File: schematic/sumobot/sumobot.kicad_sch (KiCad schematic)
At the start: 30 parts, among them J1 Conn_02x09_Odd_Even, J2 Conn_01x03, J3 Conn_02x06_Counter_Clockwise, J4 Conn_01x02_Socket, J5 Conn_01x02_Socket, J6 Conn_01x02_Socket, J7 Conn_01x07, SW3 SW_DIP_x04, U1 ROB-14450, U10 VL53L0CXV0DH1, U11 ESP32-DEVKITC-32D, U2 YAAJ_DCDC_StepDown_LM2596, U4 TPR-105F, U5 VL53L0CXV0DH1, U6 TPR-105F, U7 TPR-105F, U8 TPR-105F, U9 VL53L0CXV0DH1

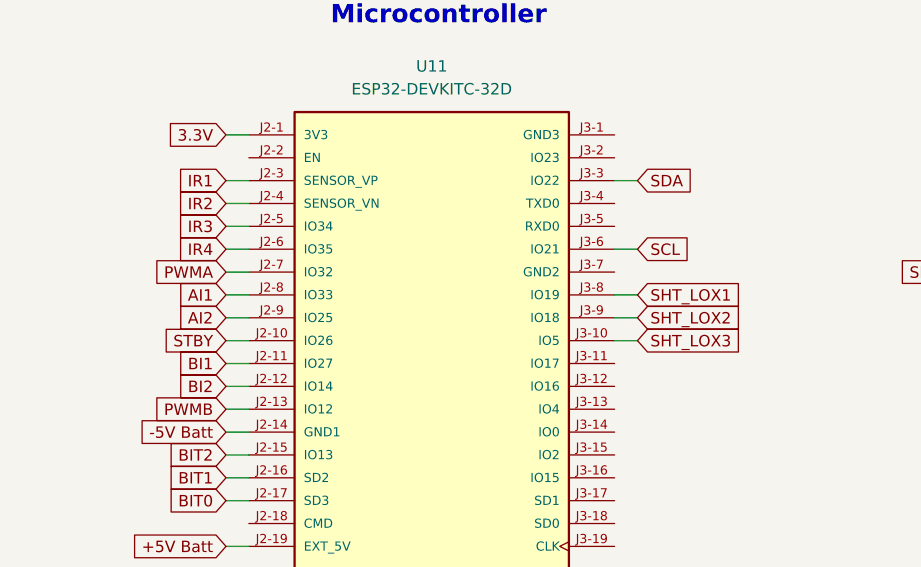
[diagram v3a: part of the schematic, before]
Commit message: feat: enhance main control logic with new sensor integration and strategy adjustments
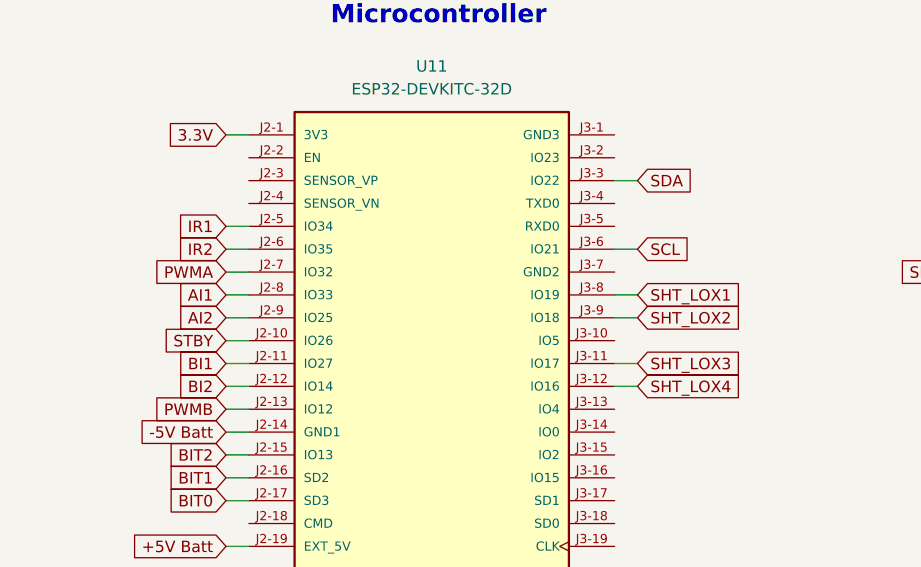
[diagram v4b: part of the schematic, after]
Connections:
- net IR1: now also U11.J2-5 (IO34); no longer U11.J2-3 (SENSOR_VP)
- net IR2: now also U11.J2-6 (IO35); no longer U11.J2-4 (SENSOR_VN)
- net IR3: no longer U11.J2-5 (IO34)
- net IR4: no longer U11.J2-6 (IO35)
- net SHT_LOX3: now also U11.J3-11 (IO17); no longer U11.J3-10 (IO5)
- net SHT_LOX4: now reaches U11.J3-12 (IO16)
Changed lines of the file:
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@@
 	(wire
 		(pts
+			(xy 176.53 215.9) (xy 179.07 215.9)
+		)
+		(stroke
+			(width 0)
+			(type default)
+		)
+	)
+	(wire
+		(pts
 			(xy 30.48 166.37) (xy 33.02 166.37)
 		)
@@
 	(wire
 		(pts
-			(xy 179.07 210.82) (xy 176.53 210.82)
-		)
-		(stroke
-			(width 0)
-			(type default)
-		)
-	)
-	(wire
-		(pts
 			(xy 233.68 162.56) (xy 234.95 162.56)
 		)
@@
 	(wire
 		(pts
+			(xy 176.53 213.36) (xy 179.07 213.36)
+		)
+		(stroke
+			(width 0)
+			(type default)
+		)
+	)
+	(wire
+		(pts
 			(xy 85.09 87.63) (xy 86.36 87.63)
 		)
@@
 	(wire
 		(pts
-			(xy 133.35 193.04) (xy 135.89 193.04)
-		)
-		(stroke
-			(width 0)
-			(type default)
-		)
-	)
-	(wire
-		(pts
 			(xy 133.35 215.9) (xy 135.89 215.9)
 		)
@@
 	(wire
 		(pts
-			(xy 133.35 195.58) (xy 135.89 195.58)
-		)
-		(stroke
-			(width 0)
-			(type default)
-		)
-	)
-	(wire
-		(pts
 			(xy 232.41 180.34) (xy 233.68 180.34)
 		)
@@
 		)
 	)
-	(global_label "IR1"
-		(shape input)
-		(at 133.35 193.04 180)
-		(fields_autoplaced yes)
-		(effects
-			(font
-				(size 1.27 1.27)
-			)
-			(justify right)
-		)
-		(property "Intersheetrefs" "${INTERSHEET_REFS}"
-			(at 127.2805 193.04 0)
-			(effects
-				(font
-					(size 1.27 1.27)
-				)
-				(justify right)
-				(hide yes)
-			)
-		)
-	)
 	(global_label "AO2"
 		(shape input)
@@
 		)
 	)
-	(global_label "IR4"
+	(global_label "IR2"
 		(shape input)
 		(at 133.35 200.66 180)
@@
 		)
 	)
+	(global_label "SHT_LOX4"
+		(shape input)
+		(at 179.07 215.9 0)
+		(fields_autoplaced yes)
+		(effects
+			(font
+				(size 1.27 1.27)
+			)
+			(justify left)
+		)
+		(property "Intersheetrefs" "${INTERSHEET_REFS}"
+			(at 191.308 215.9 0)
+			(effects
+				(font
+					(size 1.27 1.27)
+				)
+				(justify left)
+				(hide yes)
+			)
+		)
+	)
 	(global_label "-5V Batt"
 		(shape input)
@@
 		)
 	)
-	(global_label "+5V Batt"
+	(global_label "SHT_LOX3"
 		(shape input)
-		(at 283.21 81.28 0)
+		(at 179.07 213.36 0)
 		(fields_autoplaced yes)
 		(effects
@@
 		)
 		(property "Intersheetrefs" "${INTERSHEET_REFS}"
-			(at 294.9037 81.28 0)
+			(at 191.308 213.36 0)
 			(effects
 				(font
@@
 		)
 	)
-	(global_label "SHT_LOX3"
+	(global_label "+5V Batt"
 		(shape input)
-		(at 179.07 210.82 0)
+		(at 283.21 81.28 0)
 		(fields_autoplaced yes)
 		(effects
@@
 		)
 		(property "Intersheetrefs" "${INTERSHEET_REFS}"
-			(at 191.308 210.82 0)
+			(at 294.9037 81.28 0)
 			(effects
 				(font
@@
 		)
 	)
-	(global_label "IR2"
-		(shape input)
-		(at 133.35 195.58 180)
-		(fields_autoplaced yes)
-		(effects
-			(font
-				(size 1.27 1.27)
-			)
-			(justify right)
-		)
-		(property "Intersheetrefs" "${INTERSHEET_REFS}"
-			(at 127.2805 195.58 0)
-			(effects
-				(font
-					(size 1.27 1.27)
-				)
-				(justify right)
-				(hide yes)
-			)
-		)
-	)
-	(global_label "IR3"
+	(global_label "IR1"
 		(shape input)
 		(at 133.35 198.12 180)
